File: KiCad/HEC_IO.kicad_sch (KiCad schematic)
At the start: 22 parts, among them SW1 SW_DIP_x04, U12 74LS04, U17 74LS20, U22 74LS02, U30 74LS74, U31 74LS32, U32 LM79M05_TO220, U33 74LS20, U34 74LS393, U35 74LS08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

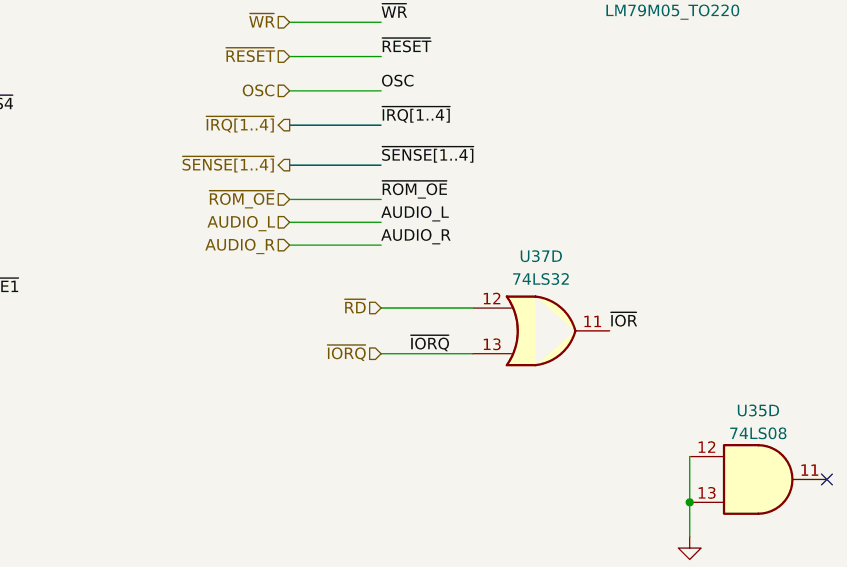
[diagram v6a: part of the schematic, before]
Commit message: Updated layout
Updated the layout of PCB. Chips on the board in this version might be in their final position.
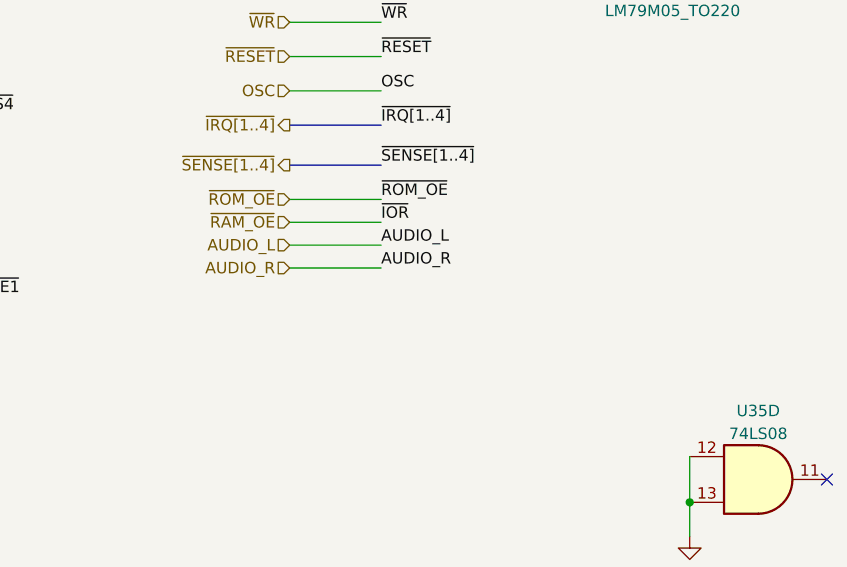
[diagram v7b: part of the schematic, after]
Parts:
- removed U37: 74LS32, Package_DIP:DIP-14_W7.62mm_Socket, symbol 74xx:74LS32
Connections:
- net ~{IOR} renamed ~{RAM_OE}

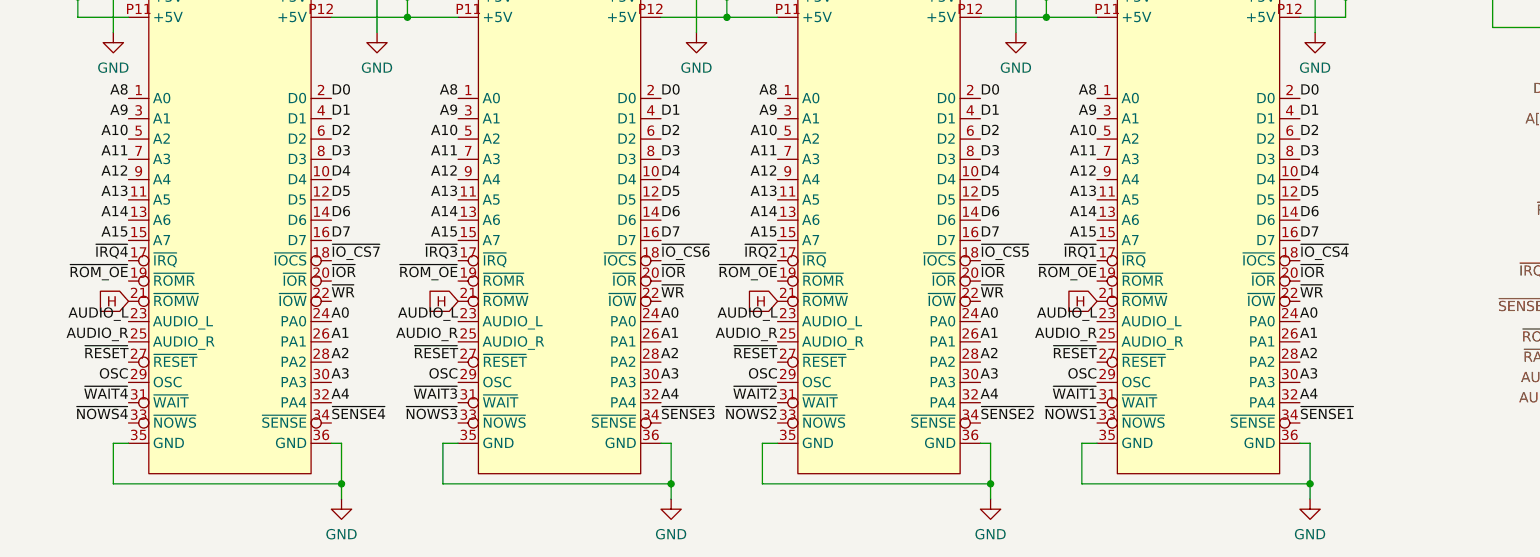
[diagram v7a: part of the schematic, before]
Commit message: New bus symbol
Updated bus symbol and footprint to simplify PCB layout.
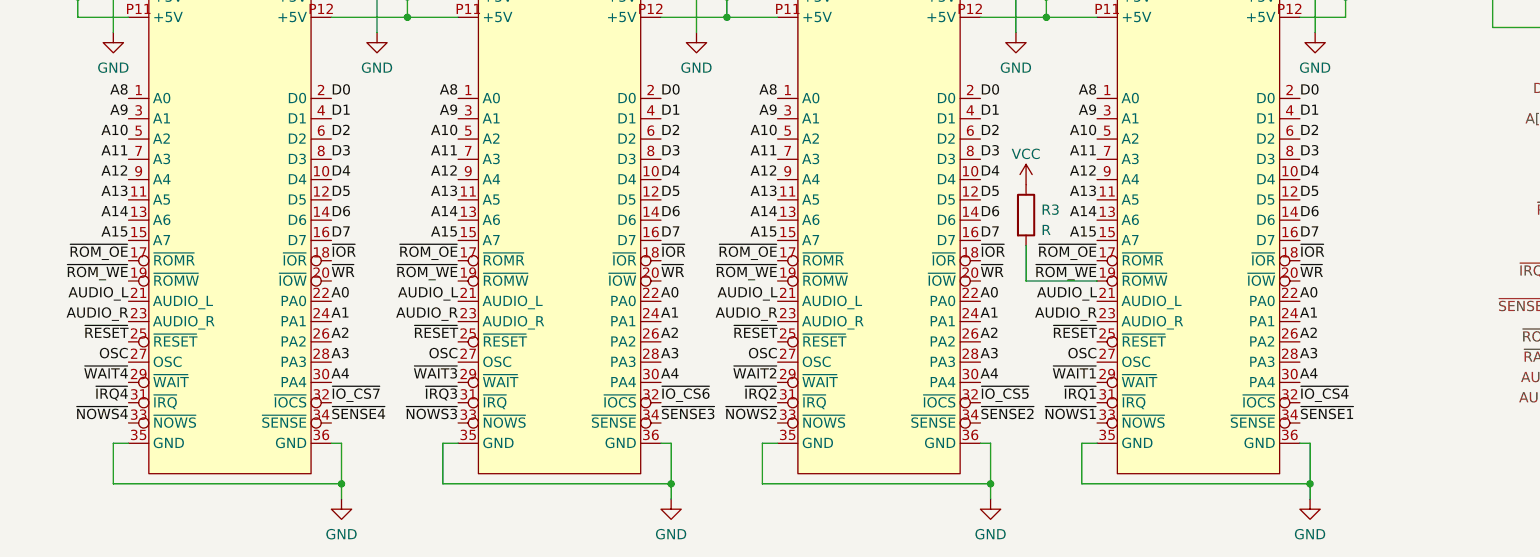
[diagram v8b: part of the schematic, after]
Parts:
- added R3: R, Resistor_THT:R_Axial_DIN0207_L6.3mm_D2.5mm_P7.62mm_Horizontal, symbol Device:R
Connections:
- net A0: now also BUS1.22 (PA0), BUS2.22 (PA0), BUS3.22 (PA0), BUS4.22 (PA0); no longer BUS1.24 (PA0), BUS2.24 (PA0), BUS3.24 (PA0), BUS4.24 (PA0)
- net A1: now also BUS1.24 (PA1), BUS2.24 (PA1), BUS3.24 (PA1), BUS4.24 (PA1); no longer BUS1.26 (PA1), BUS2.26 (PA1), BUS3.26 (PA1), BUS4.26 (PA1)
- net A2: now also BUS1.26 (PA2), BUS2.26 (PA2), BUS3.26 (PA2), BUS4.26 (PA2); no longer BUS1.28 (PA2), BUS2.28 (PA2), BUS3.28 (PA2), BUS4.28 (PA2)
- net A3: now also BUS1.28 (PA3), BUS2.28 (PA3), BUS3.28 (PA3), BUS4.28 (PA3); no longer BUS1.30 (PA3), BUS2.30 (PA3), BUS3.30 (PA3), BUS4.30 (PA3)
- net A4: now also BUS1.30 (PA4), BUS2.30 (PA4), BUS3.30 (PA4), BUS4.30 (PA4); no longer BUS1.32 (PA4), BUS2.32 (PA4), BUS3.32 (PA4), BUS4.32 (PA4)
- net AUDIO_L: now also BUS1.21 (AUDIO_L), BUS2.21 (AUDIO_L), BUS3.21 (AUDIO_L), BUS4.21 (AUDIO_L); no longer BUS1.23 (AUDIO_L), BUS2.23 (AUDIO_L), BUS3.23 (AUDIO_L), BUS4.23 (AUDIO_L)
- net AUDIO_R: now also BUS1.23 (AUDIO_R), BUS2.23 (AUDIO_R), BUS3.23 (AUDIO_R), BUS4.23 (AUDIO_R); no longer BUS1.25 (AUDIO_R), BUS2.25 (AUDIO_R), BUS3.25 (AUDIO_R), BUS4.25 (AUDIO_R)
- net H: no longer BUS1.21 (~{ROMW}), BUS2.21 (~{ROMW}), BUS3.21 (~{ROMW}), BUS4.21 (~{ROMW})
- net OSC: now also BUS1.27 (OSC), BUS2.27 (OSC), BUS3.27 (OSC), BUS4.27 (OSC); no longer BUS1.29 (OSC), BUS2.29 (OSC), BUS3.29 (OSC), BUS4.29 (OSC)
- net VCC: now also R3.1
- net ~{IO_CS4}: now also BUS1.32 (~{IOCS}); no longer BUS1.18 (~{IOCS})
- net ~{IO_CS5}: now also BUS2.32 (~{IOCS}); no longer BUS2.18 (~{IOCS})
- net ~{IO_CS6}: now also BUS3.32 (~{IOCS}); no longer BUS3.18 (~{IOCS})
- net ~{IO_CS7}: now also BUS4.32 (~{IOCS}); no longer BUS4.18 (~{IOCS})
- net ~{IRQ1}: now also BUS1.31 (~{IRQ}); no longer BUS1.17 (~{IRQ})
- net ~{IRQ2}: now also BUS2.31 (~{IRQ}); no longer BUS2.17 (~{IRQ})
- net ~{IRQ3}: now also BUS3.31 (~{IRQ}); no longer BUS3.17 (~{IRQ})
- net ~{IRQ4}: now also BUS4.31 (~{IRQ}); no longer BUS4.17 (~{IRQ})
- net ~{RAM_OE}: now also BUS1.18 (~{IOR}), BUS2.18 (~{IOR}), BUS3.18 (~{IOR}), BUS4.18 (~{IOR}); no longer BUS1.20 (~{IOR}), BUS2.20 (~{IOR}), BUS3.20 (~{IOR}), BUS4.20 (~{IOR})
- net ~{RESET}: now also BUS1.25 (~{RESET}), BUS2.25 (~{RESET}), BUS3.25 (~{RESET}), BUS4.25 (~{RESET}); no longer BUS1.27 (~{RESET}), BUS2.27 (~{RESET}), BUS3.27 (~{RESET}), BUS4.27 (~{RESET})
- net ~{ROM_OE}: now also BUS1.17 (~{ROMR}), BUS2.17 (~{ROMR}), BUS3.17 (~{ROMR}), BUS4.17 (~{ROMR}); no longer BUS1.19 (~{ROMR}), BUS2.19 (~{ROMR}), BUS3.19 (~{ROMR}), BUS4.19 (~{ROMR})
- net ~{WAIT1}: now also BUS1.29 (~{WAIT}); no longer BUS1.31 (~{WAIT})
- net ~{WAIT2}: now also BUS2.29 (~{WAIT}); no longer BUS2.31 (~{WAIT})
- net ~{WAIT3}: now also BUS3.29 (~{WAIT}); no longer BUS3.31 (~{WAIT})
- net ~{WAIT4}: now also BUS4.29 (~{WAIT}); no longer BUS4.31 (~{WAIT})
- net ~{WR}: now also BUS1.20 (~{IOW}), BUS2.20 (~{IOW}), BUS3.20 (~{IOW}), BUS4.20 (~{IOW}); no longer BUS1.22 (~{IOW}), BUS2.22 (~{IOW}), BUS3.22 (~{IOW}), BUS4.22 (~{IOW})
- new net ~{ROM_WE}: BUS1.19 (~{ROMW}), BUS2.19 (~{ROMW}), BUS3.19 (~{ROMW}), BUS4.19 (~{ROMW}), R3.2
